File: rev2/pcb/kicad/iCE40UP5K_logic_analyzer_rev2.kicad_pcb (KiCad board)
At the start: 2 copper layers, 49.6 x 52.8 mm, 80 parts, among them IC1 ICE40UP5K-SG48I, IC2 MIC5504-3.3YM5-TR, IC3 MIC5504-1.2YM5-TR, IC4 CP2102N-A02-GQFN24, IC5 W25Q40CLSNIG, J1 USB B Female Connector, J2 61300611121, J3 61201021621

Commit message: LAYOUT all components placed relatively well. Time for wiring
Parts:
- added C24: 0u1, 0u1_0603_cap_C0603C104M4RAC:CAPC1608X95N, F.Cu at (196.8, 121.1)
- added C25: 0u1, 0u1_0603_cap_C0603C104M4RAC:CAPC1608X95N, F.Cu at (196.9, 134.9)
- added C26: 0u1, 0u1_0603_cap_C0603C104M4RAC:CAPC1608X95N, F.Cu at (197.1, 148.6)
- added C27: 0u1, 0u1_0603_cap_C0603C104M4RAC:CAPC1608X95N, F.Cu at (168.2, 81.1)
- added C28: 0u1, 0u1_0603_cap_C0603C104M4RAC:CAPC1608X95N, F.Cu at (169.8, 99.9)
- added C29: 0u1, 0u1_0603_cap_C0603C104M4RAC:CAPC1608X95N, F.Cu at (175.3, 99.7)
- added C30: 0u1, 0u1_0603_cap_C0603C104M4RAC:CAPC1608X95N, F.Cu at (183.3, 90.0)
- added C31: 0u1, 0u1_0603_cap_C0603C104M4RAC:CAPC1608X95N, F.Cu at (172.3, 81.5)
- added C32: 0u1, 0u1_0603_cap_C0603C104M4RAC:CAPC1608X95N, F.Cu at (160.8, 92.2)
- added C33: 0u1, 0u1_0603_cap_C0603C104M4RAC:CAPC1608X95N, F.Cu at (161.3, 87.6)
- added C34: 4u7, 4u7_0805_cap_C0805C475K4RACTM:C0805, F.Cu at (157.1, 93.9)
- added C35: 4u7, 4u7_0805_cap_C0805C475K4RACTM:C0805, F.Cu at (157.8, 85.2)
- added C36: 0u1, 0u1_0603_cap_C0603C104M4RAC:CAPC1608X95N, F.Cu at (166.0, 81.1)
- added C37: 0u1, 0u1_0603_cap_C0603C104M4RAC:CAPC1608X95N, F.Cu at (175.3, 81.5)
- added C38: 4u7, 4u7_0805_cap_C0805C475K4RACTM:C0805, F.Cu at (173.9, 78.5)
- added D8: FTDI_RX, Blue_LED_0805_APT2012LVBC/D:LEDC2012X85N, F.Cu at (186.0, 102.8)
- added D9: FTDI_TX, Yellow_LED_0805_150080YS75000:LEDC2012X70N, F.Cu at (186.0, 100.4)
- added FB1: BLM18AG601SN1D, Ferrite_bead_BLM18AG601SN1D:BLM18SP221SN1B, F.Cu at (161.0, 86.2)
- added FB2: BLM18AG601SN1D, Ferrite_bead_BLM18AG601SN1D:BLM18SP221SN1B, F.Cu at (160.9, 93.7)
- added IC6: SN74LVC14ADBRE4, Schmitt_trigger_buffer_SN74LVC14ADBRE4:SOP65P780X200-14N, F.Cu at (193.9, 115.7)
- added IC7: SN74LVC14ADBRE4, Schmitt_trigger_buffer_SN74LVC14ADBRE4:SOP65P780X200-14N, F.Cu at (193.8, 129.5)
- added IC8: SN74LVC14ADBRE4, Schmitt_trigger_buffer_SN74LVC14ADBRE4:SOP65P780X200-14N, F.Cu at (193.8, 143.2)
- added J4: 61300821121, LIB_2x4_61300821121:J_Wurth_WR-PHD_61300821121, F.Cu at (134.4, 137.5)
- added J5: 61300821121, LIB_2x4_61300821121:J_Wurth_WR-PHD_61300821121, F.Cu at (207.5, 83.1)
- added J6: 61300311121, LIB_1x3_61300311121:J_Wurth_WR-PHD_61300311121, F.Cu at (211.8, 77.8)
- added J7: 61300621121, LIB_2x4_61300821121:J_Wurth_WR-PHD_61300621121, F.Cu at (176.2, 66.9)
- added Q1: 2N7002H6327XTSA2, NMOS_2N7002H6327XTSA2:SOT95P240X110-3N, F.Cu at (146.7, 101.8)
- added R25: 330R, Resistor_SMD:R_0603_1608Metric, F.Cu at (209.8, 116.0)
- added R26: 330R, Resistor_SMD:R_0603_1608Metric, F.Cu at (202.6, 117.8)
- added R27: 330R, Resistor_SMD:R_0603_1608Metric, F.Cu at (209.9, 119.6)
- added R28: 330R, Resistor_SMD:R_0603_1608Metric, F.Cu at (202.8, 122.2)
- added R29: 330R, Resistor_SMD:R_0603_1608Metric, F.Cu at (209.9, 123.6)
- added R30: 330R, Resistor_SMD:R_0603_1608Metric, F.Cu at (202.9, 125.7)
- added R31: 330R, Resistor_SMD:R_0603_1608Metric, F.Cu at (210.2, 127.2)
- added R32: 330R, Resistor_SMD:R_0603_1608Metric, F.Cu at (202.7, 129.3)
- added R33: 330R, Resistor_SMD:R_0603_1608Metric, F.Cu at (210.3, 130.0)
- added R34: 330R, Resistor_SMD:R_0603_1608Metric, F.Cu at (202.8, 132.4)
- added R35: 330R, Resistor_SMD:R_0603_1608Metric, F.Cu at (210.3, 134.4)
- added R36: 330R, Resistor_SMD:R_0603_1608Metric, F.Cu at (202.9, 136.0)
- added R37: 330R, Resistor_SMD:R_0603_1608Metric, F.Cu at (210.3, 138.2)
- added R38: 330R, Resistor_SMD:R_0603_1608Metric, F.Cu at (203.0, 140.2)
- added R39: 330R, Resistor_SMD:R_0603_1608Metric, F.Cu at (210.1, 141.7)
- added R40: 330R, Resistor_SMD:R_0603_1608Metric, F.Cu at (202.7, 144.8)
- added R41: 100k, Resistor_SMD:R_0603_1608Metric, F.Cu at (207.6, 115.2)
- added R42: 100k, Resistor_SMD:R_0603_1608Metric, F.Cu at (200.3, 117.1)
- added R43: 100k, Resistor_SMD:R_0603_1608Metric, F.Cu at (207.6, 118.8)
- added R44: 100k, Resistor_SMD:R_0603_1608Metric, F.Cu at (200.5, 121.5)
- added R45: 100k, Resistor_SMD:R_0603_1608Metric, F.Cu at (207.7, 123.0)
- added R46: 100k, Resistor_SMD:R_0603_1608Metric, F.Cu at (200.6, 125.0)
- added R47: 100k, Resistor_SMD:R_0603_1608Metric, F.Cu at (208.0, 126.4)
- added R48: 100k, Resistor_SMD:R_0603_1608Metric, F.Cu at (200.4, 128.8)
- added R49: 100k, Resistor_SMD:R_0603_1608Metric, F.Cu at (207.8, 129.7)
- added R50: 100k, Resistor_SMD:R_0603_1608Metric, F.Cu at (200.6, 132.4)
- added R51: 100k, Resistor_SMD:R_0603_1608Metric, F.Cu at (208.0, 134.5)
- added R52: 100k, Resistor_SMD:R_0603_1608Metric, F.Cu at (200.6, 136.3)
- added R53: 100k, Resistor_SMD:R_0603_1608Metric, F.Cu at (208.1, 137.4)
- added R54: 100k, Resistor_SMD:R_0603_1608Metric, F.Cu at (200.7, 140.1)
- added R55: 100k, Resistor_SMD:R_0603_1608Metric, F.Cu at (207.7, 141.7)
- added R56: 100k, Resistor_SMD:R_0603_1608Metric, F.Cu at (200.5, 144.9)
- added R57: 10k, Resistor_SMD:R_0603_1608Metric, F.Cu at (174.7, 103.9)
- added R58: 10k, Resistor_SMD:R_0603_1608Metric, F.Cu at (177.3, 103.9)
- added R59: 10k, Resistor_SMD:R_0603_1608Metric, F.Cu at (179.8, 103.9)
- added R60: 10k, Resistor_SMD:R_0603_1608Metric, F.Cu at (188.1, 92.8)
- added R61: 10k, Resistor_SMD:R_0603_1608Metric, F.Cu at (188.1, 91.3)
- added R62: 10k, Resistor_SMD:R_0603_1608Metric, F.Cu at (188.0, 89.8)
- added R63: 10k, Resistor_SMD:R_0603_1608Metric, F.Cu at (188.1, 88.2)
- added R64: 10k, Resistor_SMD:R_0603_1608Metric, F.Cu at (188.1, 86.7)
- added R65: 100R, Resistor_SMD:R_0603_1608Metric, F.Cu at (141.2, 124.4)
- added R66: 100R, Resistor_SMD:R_0603_1608Metric, F.Cu at (141.2, 121.8)
- added R67: 100R, Resistor_SMD:R_0603_1608Metric, F.Cu at (141.2, 116.7)
- added R68_unp1: 0R, Resistor_SMD:R_0805_2012Metric, F.Cu at (141.4, 126.9)
- added R69: 100R, Resistor_SMD:R_0603_1608Metric, F.Cu at (141.9, 137.6)
- added R70: 100R, Resistor_SMD:R_0603_1608Metric, F.Cu at (141.9, 140.0)
- added R71: 100R, Resistor_SMD:R_0603_1608Metric, F.Cu at (141.9, 142.6)
- added R72: 100R, Resistor_SMD:R_0603_1608Metric, F.Cu at (141.9, 145.1)
- added R73: 0R, Resistor_SMD:R_0805_2012Metric, F.Cu at (179.5, 71.8)
- added R74: 0R, Resistor_SMD:R_0805_2012Metric, F.Cu at (194.5, 71.8)
- added S2: L101011MS02Q, Slide_switch_SPST_ON/OFF_L101011MS02Q:L101011MS02Q, F.Cu at (160.4, 72.3)
- added TP18: VCC_PLL, TestPoint:TestPoint_Pad_D1.0mm, F.Cu at (164.6, 129.9)
- added TP21: GND, TestPoint:TestPoint_Pad_D1.0mm, F.Cu at (164.1, 86.3)
- added TP22: VS_OSC, TestPoint:TestPoint_Pad_D1.0mm, F.Cu at (164.2, 77.2)
- added TP23: VPHY, TestPoint:TestPoint_Pad_D1.0mm, F.Cu at (159.4, 81.3)
- added TP24: REF, TestPoint:TestPoint_Pad_D1.0mm, F.Cu at (163.7, 89.1)
- added TP25: VPLL, TestPoint:TestPoint_Pad_D1.0mm, F.Cu at (156.1, 96.9)
- added TP26: FTDI_VCORE, TestPoint:TestPoint_Pad_D1.0mm, F.Cu at (182.4, 95.0)
- added TP27: TEST, TestPoint:TestPoint_Pad_D1.0mm, F.Cu at (158.8, 96.9)
- added TP28: RESET#, TestPoint:TestPoint_Pad_D1.0mm, F.Cu at (161.9, 99.2)
- added TP29: FTDI_VCCIO, TestPoint:TestPoint_Pad_D1.0mm, F.Cu at (180.6, 90.0)
- added TP33: GND, TestPoint:TestPoint_Pad_D1.0mm, F.Cu at (182.1, 85.3)
- added Y1: 830208214809, 12MHz_CMOS_clock_830208214809:830208214809, F.Cu at (163.3, 83.0)
- C6: value 4u7 -> 3u3
- IC4: value CP2102N-A02-GQFN24 -> FT2232HL-TRAY; footprint UART_USB_bridge_CP2102N-A02-GQFN24:QFN50P400X400X80-25N-D -> UART_USB_bridge_FT2232HL:QFP50P1200X1200X160-64N
- J3: value 61201021621 -> 61202021621; footprint 10_pin_2x5_shroued_header_61201021621:SHDR10W64P254_2X5_2036X885X925P -> 20_pin_2x10_shrouded_header_61202021621:SHDR20W64P254_2X10_3306X910X885P
- R14: value 22R -> 100R
- R2: value 1k -> 12k
- R21: value 680R -> 330R
- R22: value 330R -> 680R
- R24: value 470R -> 680R
- R3: value 22k1 -> 10k
- R4: value 47k5 -> 4k7
- R5: value 10k -> 1k
- R6, R7: value 10k -> 680R
- S1: value 418121270801 -> OS102011MA1QN1; footprint 1pole_DIP_switch_418121270801:418121270801 -> Slide_switch_SPDT_ON/ON_OS102011MA1QN1:OS102011MA1QN1
- TP10: value CH0_sampling -> VREGOUT
- TP11: value GND -> VCCIO; footprint TestPoint:TestPoint_Pad_D1.5mm -> TestPoint:TestPoint_Pad_D1.0mm
- TP12: value GND -> FTDI_VREGIN
- TP15: value GND -> VCC
- TP7: value SPI_SCK -> PWREN#
- TP8: value FPGA_UART_TX -> SUSPEND#
- TP9: value FPGA_UART_RX -> PWRSAV#
- moved TP3 78.5 mm to (197.7, 69.5)
- moved TP1 69.4 mm to (171.1, 64.4)
- moved TP4 66.9 mm to (173.2, 67.3)
- moved TP5 64.6 mm to (218.6, 80.7)
- moved TP6 63.8 mm to (214.9, 80.6)
- moved TP2 61.3 mm to (181.6, 74.7)
- moved TP13 59.7 mm to (211.0, 80.7)
- moved F1 57.0 mm to (137.1, 74.4), turned to 0 degrees
- moved C2 56.4 mm to (167.7, 70.9), turned to 90 degrees
- moved C5 55.3 mm to (188.6, 70.2), turned to 90 degrees
- moved C22 55.0 mm to (176.1, 72.2), turned to -90 degrees
- moved C4 54.7 mm to (182.3, 71.0)
- moved FL1 54.0 mm to (143.3, 74.1), turned to 90 degrees
- moved IC3 53.9 mm to (185.6, 72.0)
- moved IC2 52.6 mm to (170.7, 71.7), turned to 0 degrees
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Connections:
- C13 pad 1: Net-(IC1-VCCPLL) -> /FPGA_VCCPLL
- C21 pad 1: Net-(IC1-VCCPLL) -> /FPGA_VCCPLL
- C22 pad 1: +3V3 -> Net-(IC2-VOUT)
- C23 pad 1: +1V2 -> Net-(IC3-VOUT)
- C3 pad 1: +3V3 -> Net-(IC2-VOUT)
- C5 pad 1: +1V2 -> Net-(IC3-VOUT)
- C6 pad 1: +3V3 -> +1V8
- C7 pad 1: +3V3 -> +1V8
- C8 pad 1: +3V3 -> +1V8
- D2 pad 1: Net-(D2-K_1) -> /USB_D-
- D2 pad 2: Net-(D2-K_2) -> /USB_D+
- D4 pad 1: GND -> Net-(D4-K)
- FL1 pad 1: +5V -> Net-(FL1-Pad1)
- IC1 pad 18: unconnected-(IC1-IOB_31B-Pad18) -> Net-(IC1-IOB_31B)
- IC1 pad 19: unconnected-(IC1-IOB_29B-Pad19) -> Net-(IC1-IOB_29B)
- IC1 pad 2: unconnected-(IC1-IOB_6A-Pad2) -> /RTS#
- IC1 pad 20: unconnected-(IC1-IOB_25B_G3-Pad20) -> Net-(IC1-IOB_25B_G3)
- IC1 pad 21: unconnected-(IC1-IOB_23B-Pad21) -> Net-(IC1-IOB_23B)
- IC1 pad 27: unconnected-(IC1-IOT_38B-Pad27) -> /LA15
- IC1 pad 28: unconnected-(IC1-IOT_41A-Pad28) -> /LA14
- IC1 pad 29: Net-(IC1-VCCPLL) -> /FPGA_VCCPLL
- IC1 pad 3: Net-(IC1-IOB_9B) -> /FPGA_UART_RX
- IC1 pad 31: unconnected-(IC1-IOT_42B-Pad31) -> /LA13
- IC1 pad 32: unconnected-(IC1-IOT_43A-Pad32) -> /LA12
- IC1 pad 34: unconnected-(IC1-IOT_44B-Pad34) -> /LA11
- IC1 pad 35: unconnected-(IC1-IOT_46B_G0-Pad35) -> /LA10
- IC1 pad 36: /LA7 -> /LA9
- IC1 pad 37: unconnected-(IC1-IOT_45A_G1-Pad37) -> /LA8
- IC1 pad 38: /LA6 -> /LA7
- IC1 pad 4: Net-(IC1-IOB_8A) -> /FPGA_UART_TX
- IC1 pad 42: /LA5 -> /LA6
- IC1 pad 43: /LA4 -> /LA5
- IC1 pad 44: unconnected-(IC1-IOB_3B_G6-Pad44) -> /LA4
- IC1 pad 6: unconnected-(IC1-IOB_13B-Pad6) -> /CTS#
- IC1 pad 8: Net-(IC1-CRESET_B) -> /CRESET_B
- IC2 pad 5: +3V3 -> Net-(IC2-VOUT)
- IC3 pad 5: +1V2 -> Net-(IC3-VOUT)
- IC4 pad 1: Net-(IC4-RI_/_CLK) -> GND
- IC4 pad 10: unconnected-(IC4-NC_1-Pad10) -> GND
- IC4 pad 11: unconnected-(IC4-GPIO.3_/_WAKEUP-Pad11) -> GND
- IC4 pad 12: unconnected-(IC4-GPIO.2_/_RS485-Pad12) -> +1V8
- IC4 pad 13: unconnected-(IC4-GPIO.1_/_RXT-Pad13) -> GND
- IC4 pad 14: unconnected-(IC4-GPIO.0_/_TXT-Pad14) -> /FTDI_RESET#
- IC4 pad 15: unconnected-(IC4-SUSPENDB-Pad15) -> GND
- IC4 pad 16: unconnected-(IC4-NC_2-Pad16) -> /FPGA_UART_RX
- IC4 pad 17: unconnected-(IC4-SUSPEND-Pad17) -> /FPGA_UART_TX
- IC4 pad 18: Net-(IC4-CTS) -> /RTS#
- IC4 pad 19: unconnected-(IC4-RTS-Pad19) -> /CTS#
- IC4 pad 2: GND -> /OSCI
- IC4 pad 20: Net-(IC1-IOB_8A) -> +3V3
- IC4 pad 21: Net-(IC1-IOB_9B) -> unconnected-(IC4-ADBUS4-Pad21)
- IC4 pad 22: Net-(IC4-DSR) -> Net-(IC4-ADBUS5)
- IC4 pad 23: unconnected-(IC4-DTR-Pad23) -> Net-(IC4-ADBUS6)
- IC4 pad 24: Net-(IC4-DCD) -> Net-(IC4-ADBUS7)
- IC4 pad 3: Net-(D2-K_2) -> unconnected-(IC4-OSCO-Pad3)
- IC4 pad 4: Net-(D2-K_1) -> /FTDI_VPHY
- IC4 pad 5: +3V3 -> GND
- IC4 pad 6: +3V3 -> /FTDI_REF
- IC4 pad 7: +3V3 -> /USB_D-
- IC4 pad 8: Net-(IC4-VBUS) -> /USB_D+
- IC4 pad 9: Net-(IC4-RSTB) -> /FTDI_VPLL
- J1 pad 2: Net-(D2-K_1) -> /USB_D-
- J1 pad 3: Net-(D2-K_2) -> /USB_D+
- J2 pad 3: /SPI_CLK -> Net-(J2-Pad3)
- J2 pad 4: /SPI_MOSI -> Net-(J2-Pad4)
- J2 pad 6: /SPI_CSn -> Net-(J2-Pad6)
- J3 pad 10: /LA7 -> /LA7_raw
- J3 pad 2: /LA0 -> /LA0_raw
- J3 pad 3: /LA1 -> /LA1_raw
- J3 pad 4: /LA2 -> /LA2_raw
- J3 pad 5: /LA3 -> /LA3_raw
- J3 pad 7: /LA4 -> /LA4_raw
- J3 pad 8: /LA5 -> /LA5_raw
- J3 pad 9: /LA6 -> /LA6_raw
- R1 pad 2: Net-(IC1-CRESET_B) -> /CRESET_B
- R16 pad 1: +3V3 -> /SPI_MOSI
- R16 pad 2: Net-(J2-Pad2) -> GND
- R17 pad 1: +1V2 -> /FPGA_VCCPLL
- R17 pad 2: Net-(IC1-VCCPLL) -> +1V2
- R19 pad 1: +3V3 -> /SPI_CSn
- R19 pad 2: /SPI_CSn -> +3V3
- R2 pad 1: +3V3 -> /FTDI_REF
- R2 pad 2: Net-(IC4-RSTB) -> GND
- R21 pad 2: /CDONE -> +3V3
- R3 pad 1: +5V -> GND
- R3 pad 2: Net-(IC4-VBUS) -> /FTDI_PWRSAV
- R4 pad 1: Net-(IC4-VBUS) -> /FTDI_PWRSAV
- R4 pad 2: GND -> +5V
- R5 pad 2: Net-(IC4-RI_/_CLK) -> /FTDI_RESET#
- R6 pad 1: Net-(IC4-DCD) -> +3V3
- R6 pad 2: +3V3 -> Net-(D8-A)
- R7 pad 2: Net-(IC4-DSR) -> Net-(D9-A)
- R8 pad 1: Net-(IC4-CTS) -> Net-(Y1-ENABLE/DISABLE)
- S1 pad 1: Net-(IC1-CRESET_B) -> GND
- S1 pad 2: GND -> /CRESET_B
- TP10 pad 1: /LA0 -> +1V8
- TP11 pad 1: GND -> +3V3
- TP12 pad 1: GND -> +3V3
- TP15 pad 1: GND -> +1V2
- TP6 pad 1: Net-(IC1-CRESET_B) -> /CRESET_B
- TP7 pad 1: /SPI_CLK -> Net-(IC4-PWREN#)
- TP8 pad 1: Net-(IC1-IOB_8A) -> Net-(IC4-SUSPEND#)
- TP9 pad 1: Net-(IC1-IOB_9B) -> /FTDI_PWRSAV
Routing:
- net /USB_D-: track 0.00 -> 80.0 mm
- net /USB_D+: track 0.00 -> 79.7 mm, vias 0 -> 2
- net Net-(D2-K_1): track 59.1 -> 0.00 mm
- net Net-(D2-K_2): track 58.4 -> 0.00 mm, vias 2 -> 0
- net Net-(IC1-IOB_9B): track 26.0 -> 0.00 mm
- net /FPGA_UART_RX: track 0.00 -> 25.7 mm
- net /CRESET_B: track 0.00 -> 20.6 mm
- net Net-(IC1-CRESET_B): track 20.3 -> 0.00 mm
- net (no net): track 0.00 -> 19.9 mm
- net /LA9: track 0.00 -> 13.2 mm
- net Net-(IC1-IOB_8A): track 11.7 -> 0.00 mm
- net /FPGA_UART_TX: track 0.00 -> 11.7 mm
- net /LA4: track 9.28 -> 0.00 mm
- net /UART_TX_LED: track 13.3 -> 4.14 mm
- net Net-(IC1-VCCPLL): track 7.31 -> 0.00 mm
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- removed copper zone on B.Cu, net GND
- removed copper zone on F.Cu, net GND
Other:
- board size 49.6 x 52.8 mm -> 89.8 x 89.3 mm
- board text added: "3V3"
- board text added: "CLK"
- board text added: "CONFIG_HDR"
- board text added: "CSn"
- board text added: "DBG_LEDs"
- board text added: "External rail injection for debugging only!"
- board text added: "FPGA_DBG"
- board text added: "FTDI_UART_STATUS"
- board text added: "GND"
- board text added: "Logic Analyzer iCE40 UP5K Revision 2 23-06-2026 //JKO"
- board text added: "MISO"
- board text added: "MOSI"
- board text added: "POWER_RAILS_HDR"
- board text added: "PROG_HDR"
- board text added: "UART_HDR"
- board text removed: "Logic Analyzer iCE40 UP5K Revision 2 XX-XX-2026 //JKO"

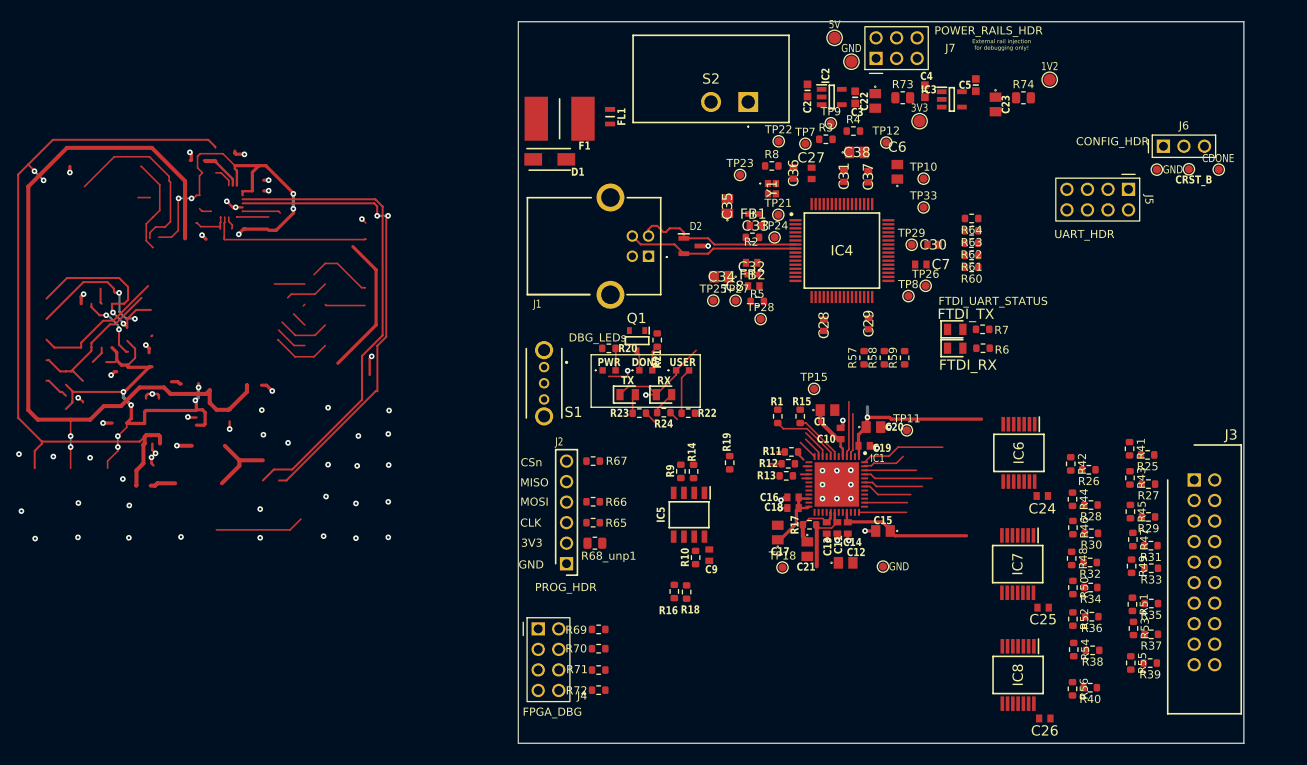
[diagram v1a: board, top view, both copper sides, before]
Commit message: LAYOUT in the works. SPI lines connected last
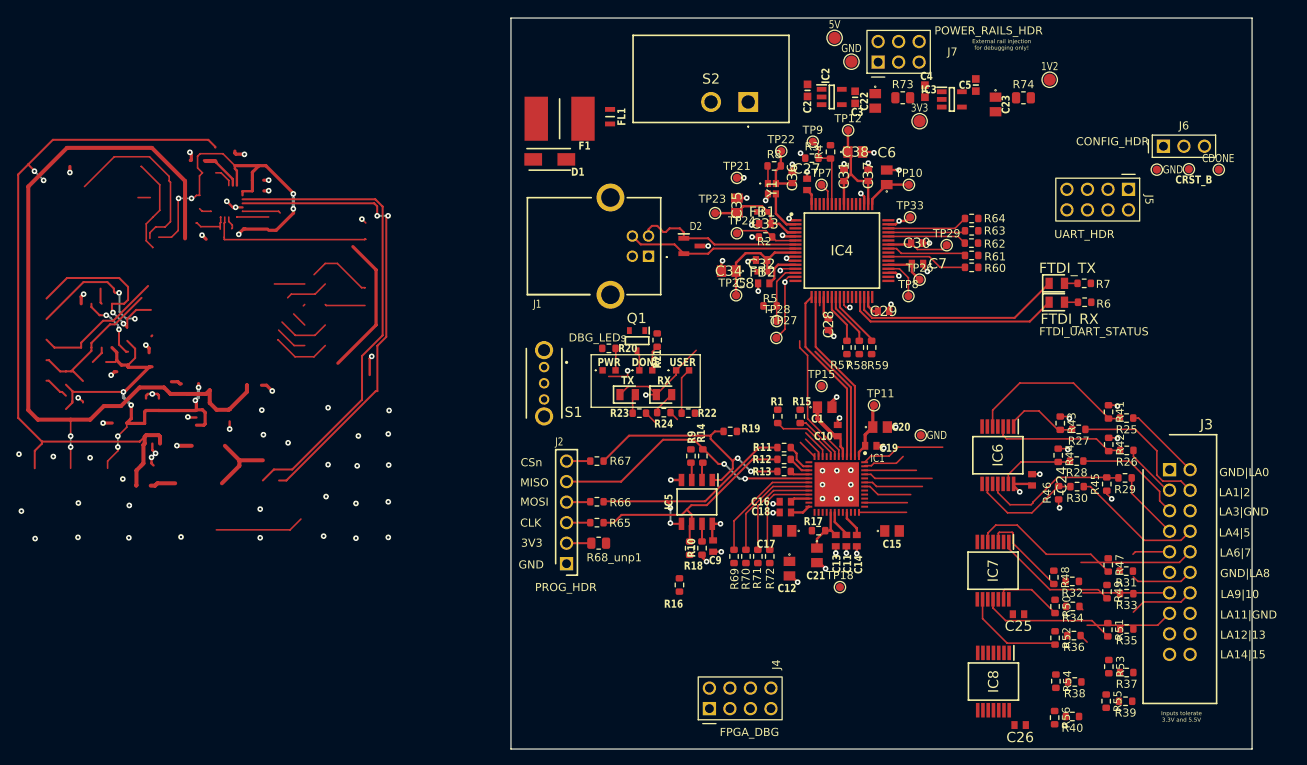
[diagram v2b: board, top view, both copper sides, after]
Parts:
- moved R72 26.9 mm to (163.1, 128.5), turned to 90 degrees
- moved R71 24.2 mm to (161.6, 128.5), turned to 90 degrees
- moved J4 23.4 mm to (155.6, 147.4), turned to 90 degrees
- moved R70 21.5 mm to (160.1, 128.5), turned to 90 degrees
- moved R69 19.0 mm to (158.6, 128.5), turned to 90 degrees
- moved TP14 16.9 mm to (181.8, 113.5)
- moved R6 13.8 mm to (202.0, 97.1)
- moved R7 13.8 mm to (202.0, 94.7)
- moved D8 13.8 mm to (198.6, 97.1)
- moved D9 13.8 mm to (198.6, 94.7)
- moved R27 11.0 mm to (201.3, 112.8)
- moved R43 11.0 mm to (199.0, 112.0)
- moved TP18 7.52 mm to (171.8, 132.3)
- moved C12 6.99 mm to (165.5, 130.0), turned to -90 degrees
- moved TP21 6.87 mm to (159.0, 81.7)
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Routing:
- net GND: track 73.0 -> 129.4 mm, vias 71 -> 110
- net /SPI_MISO: track 17.3 -> 50.7 mm, vias 2 -> 4
- net /SPI_CSn: track 23.7 -> 54.8 mm, vias 2 -> 4
- net /SPI_CLK: track 20.1 -> 47.7 mm
- net /SPI_MOSI: track 17.5 -> 45.1 mm, vias 0 -> 2
- net /FTDI_TX_LED#: track 0.00 -> 26.7 mm
- net /FTDI_RX_LED#: track 0.00 -> 26.6 mm
- net /RTS#: track 0.00 -> 21.8 mm
- net Net-(IC6-3A): track 0.00 -> 21.0 mm
- net Net-(IC7-3A): track 0.00 -> 18.8 mm
- net +1V8: track 0.00 -> 18.1 mm
- net Net-(IC6-5A): track 0.00 -> 18.1 mm
- net /LA2_raw: track 0.00 -> 17.8 mm
- net /CTS#: track 0.00 -> 17.4 mm
- net Net-(IC7-5A): track 0.00 -> 16.7 mm
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- added copper zone on In1.Cu, net GND
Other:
- board size 89.8 x 89.3 mm -> 91.7 x 90.5 mm
- copper layers 2 -> 4
- board text added: "${REFERENCE}"
- board text added: "GND|LA0"
- board text added: "GND|LA8"
- board text added: "Inputs tolerate 3.3V and 5.5V"
- board text added: "LA11|GND"
- board text added: "LA12|13"
- board text added: "LA14|15"
- board text added: "LA1|2"
- board text added: "LA3|GND"
- board text added: "LA4|5"
- board text added: "LA6|7"
- board text added: "LA9|10"

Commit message: LAYOUT. update to SPI lines.
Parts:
- moved J4 7.76 mm to (156.8, 139.7)
- moved R16 4.55 mm to (151.7, 127.5)
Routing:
- net GND: track 129.4 -> 132.0 mm, vias 110 -> 112
- net /SPI_MOSI: track 45.1 -> 47.5 mm
- net +3V3: track 177.4 -> 178.4 mm, vias 14 -> 15
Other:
- board text added: "INPUT_HDR"
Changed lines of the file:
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@@
 		(tags "resistor")
 		(property "Reference" "R69"
-			(at -2.7818 0.0716 90)
+			(at -3.0358 -0.2032 90)
 			(layer "F.SilkS")
 			(effects
@@
 		(tags "Capacitor")
 		(property "Reference" "C9"
-			(at -1.775 0.275 180)
+			(at -2.185966 0.2032 270)
 			(layer "F.SilkS")
 			(effects
@@
 		(tags "resistor")
 		(property "Reference" "R72"
-			(at -2.731 0.06 90)
+			(at -2.985 -0.2148 90)
 			(layer "F.SilkS")
 			(effects
@@
 		(tags "resistor")
 		(property "Reference" "R10"
-			(at -0.025 1.3 90)
+			(at 3.252766 -0.1016 270)
 			(layer "F.SilkS")
 			(effects
@@
 		(tags "resistor")
 		(property "Reference" "R18"
-			(at 2.1844 -0.4572 180)
+			(at 3.239 -0.1524 270)
 			(layer "F.SilkS")
 			(effects
@@
 	(footprint "Resistor_SMD:R_0603_1608Metric"
 		(layer "F.Cu")
-		(at 151.892 132.066234 -90)
+		(at 151.6888 127.5202 -90)
 		(descr "Resistor SMD 0603 (1608 Metric), square (rectangular) end terminal, IPC-7351 nominal, (Body size source: IPC-SM-782 page 72, https://www.pcb-3d.com/wordpress/wp-content/uploads/ipc-sm-782a_amendment_1_and_2.pdf), generated with kicad-footprint-generator")
 		(tags "resistor")
 		(property "Reference" "R16"
-			(at 2.355633 0.73 0)
+			(at 2.7818 0.0508 90)
 			(layer "F.SilkS")
 			(effects
@@
 		(tags "resistor")
 		(property "Reference" "R70"
-			(at -2.7818 0 90)
+			(at -3.0358 -0.2748 90)
 			(layer "F.SilkS")
 			(effects
@@
 		(tags "resistor")
 		(property "Reference" "R71"
-			(at -2.6802 -0.0716 90)
+			(at -2.9342 -0.3464 90)
 			(layer "F.SilkS")
 			(effects
@@
 		(tags "resistor")
 		(property "Reference" "R68_unp1"
-			(at 1.9163 1.778 0)
+			(at 5.2691 0.2032 0)
 			(layer "F.SilkS")
 			(effects
@@
 	(footprint "LIB_2x4_61300821121:J_Wurth_WR-PHD_61300821121"
 		(layer "F.Cu")
-		(at 155.6004 147.3708 90)
+		(at 156.7688 139.7 90)
 		(descr "2.54 mm THT Dual Pin Header, body 10.16x5.08x11.54mm, https://www.we-online.com/en/components/products/datasheet/61300821121?ki")
 		(tags "THT")
 		(property "Reference" "J4"
-			(at 5.4356 8.2804 90)
+			(at 3.0988 -2.8956 0)
 			(unlocked yes)
 			(layer "F.SilkS")
@@
 		(layer "Edge.Cuts")
 	)
+	(gr_text "INPUT_HDR"
+		(at 211.6328 150.622 0)
+		(layer "F.SilkS")
+		(effects
+			(font
+				(size 1 1)
+				(thickness 0.1)
+			)
+			(justify left bottom)
+		)
+	)
 	(gr_text "FPGA_DBG"
-		(at 156.8704 150.876 0)
+		(at 155.1432 143.3068 0)
 		(layer "F.SilkS")
 		(effects
@@
 	)
 	(segment
+		(start 163.9968 124.6268)
+		(end 163.4744 124.1044)
+		(width 0.3)
+		(layer "F.Cu")
+		(net 46)
+	)
+	(segment
 		(start 171.2468 128.5748)
 		(end 171.2468 128.422976)
@@
 	)
 	(segment
+		(start 151.6888 128.3452)
+		(end 150.6484 128.3452)
+		(width 0.25)
+		(layer "F.Cu")
+		(net 46)
+	)
+	(segment
 		(start 165.746 130.948)
 		(end 165.5064 130.948)
@@
 	)
 	(segment
+		(start 163.9968 125.3744)
+		(end 163.9968 124.6268)
+		(width 0.3)
+		(layer "F.Cu")
+		(net 46)
+	)
+	(segment
 		(start 162.8496 84.1908)
 		(end 162.8496 83.6676)
@@
 	)
 	(segment
+		(start 150.6484 128.3452)
+		(end 150.622 128.3716)
+		(width 0.25)
+		(layer "F.Cu")
+		(net 46)
+	)
+	(segment
 		(start 86.5616 117.0284)
 		(end 86.8116 117.2784)
@@
 	)
 	(via
+		(at 150.622 128.3716)
+		(size 0.7)
+		(drill 0.3)
+		(layers "F.Cu" "B.Cu")
+		(net 46)
+	)
+	(via
 		(at 87.0616 115.7784)
 		(size 0.7)
@@
 		(net 46)
 	)
+	(via
+		(at 163.4744 124.1044)
+		(size 0.7)
+		(drill 0.3)
+		(layers "F.Cu" "B.Cu")
+		(net 46)
+	)
 	(segment
 		(start 72.1106 115.4684)
@@
 	)
 	(segment
+		(start 153.162 129.1844)
+		(end 153.2636 129.286)
+		(width 0.25)
+		(layer "F.Cu")
+		(net 48)
+	)
+	(segment
 		(start 114.3508 99.8982)
 		(end 109.6206 104.6284)
@@
 	)
 	(segment
+		(start 153.162 128.3452)
+		(end 153.162 129.1844)
+		(width 0.25)
+		(layer "F.Cu")
+		(net 48)
+	)
+	(segment
 		(start 97.3616 88.6784)
 		(end 97.3616 88.604736)
@@
 	)
 	(via
+		(at 153.2636 129.286)
+		(size 0.7)
+		(drill 0.3)
+		(layers "F.Cu" "B.Cu")
+		(net 48)
+	)
+	(via
 		(at 83.0866 108.1784)
 		(size 0.7)
@@
 	)
 	(segment
+		(start 152.146 126.238)
+		(end 151.6888 126.6952)
+		(width 0.25)
+		(layer "F.Cu")
+		(net 74)
+	)
+	(segment
 		(start 150.8644 124.4992)
 		(end 150.7744 124.4092)
@@
 		(width 0.25)
 		(layer "F.Cu")
+		(net 74)
+	)
+	(segment
+		(start 152.146 124.4992)
+		(end 152.146 126.238)
+		(width 0.25)
+		(layer "F.Cu")
